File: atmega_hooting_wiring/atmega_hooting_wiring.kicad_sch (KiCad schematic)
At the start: 3 parts, among them U2 ATmega328-P

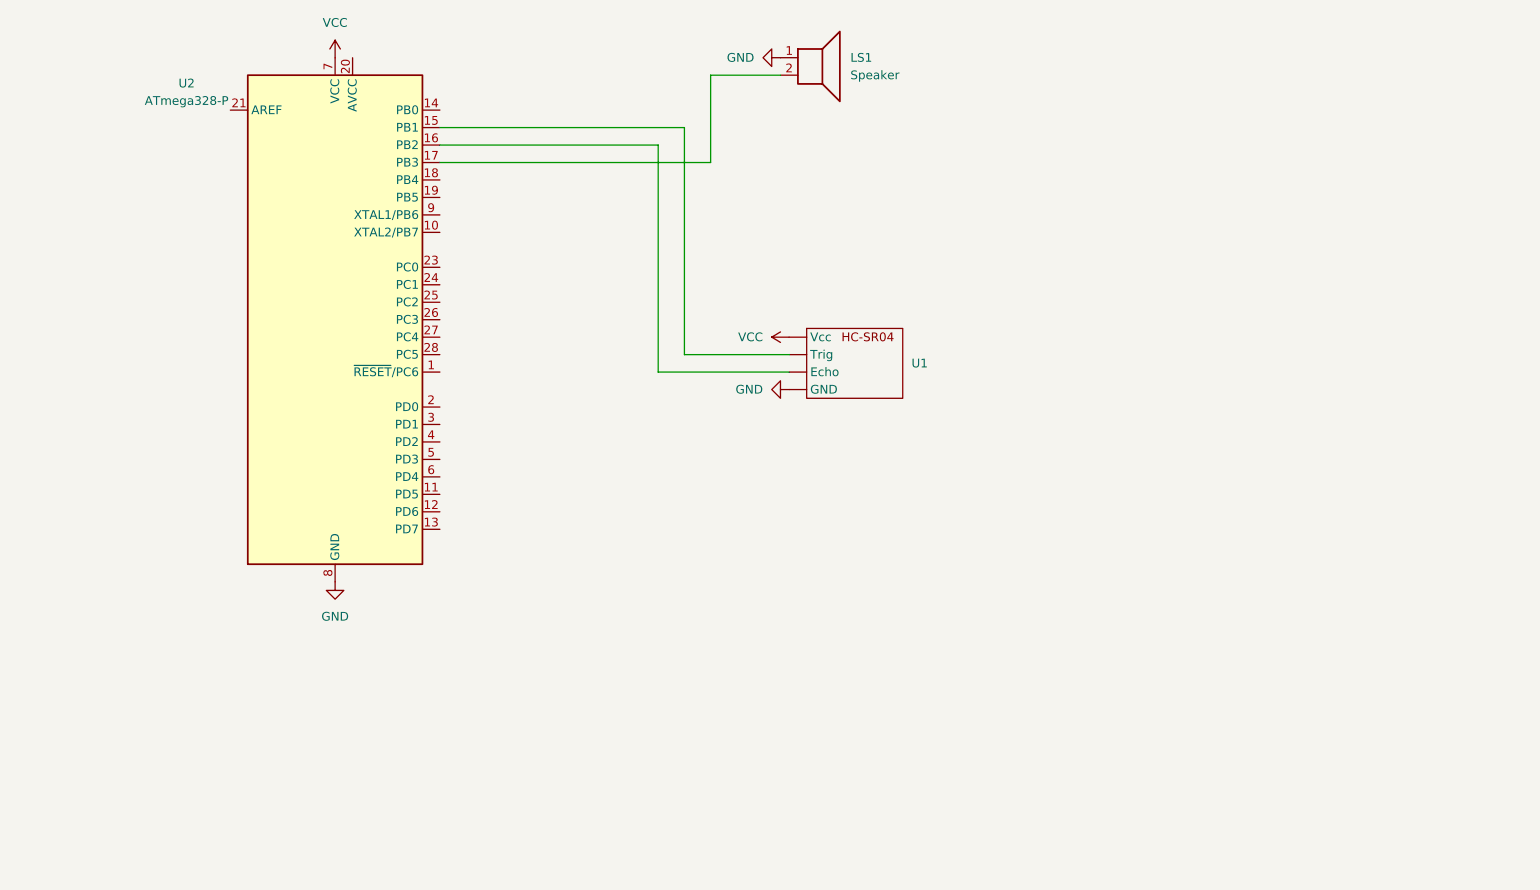
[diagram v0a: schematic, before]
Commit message: add pcb and wiring schematic for production
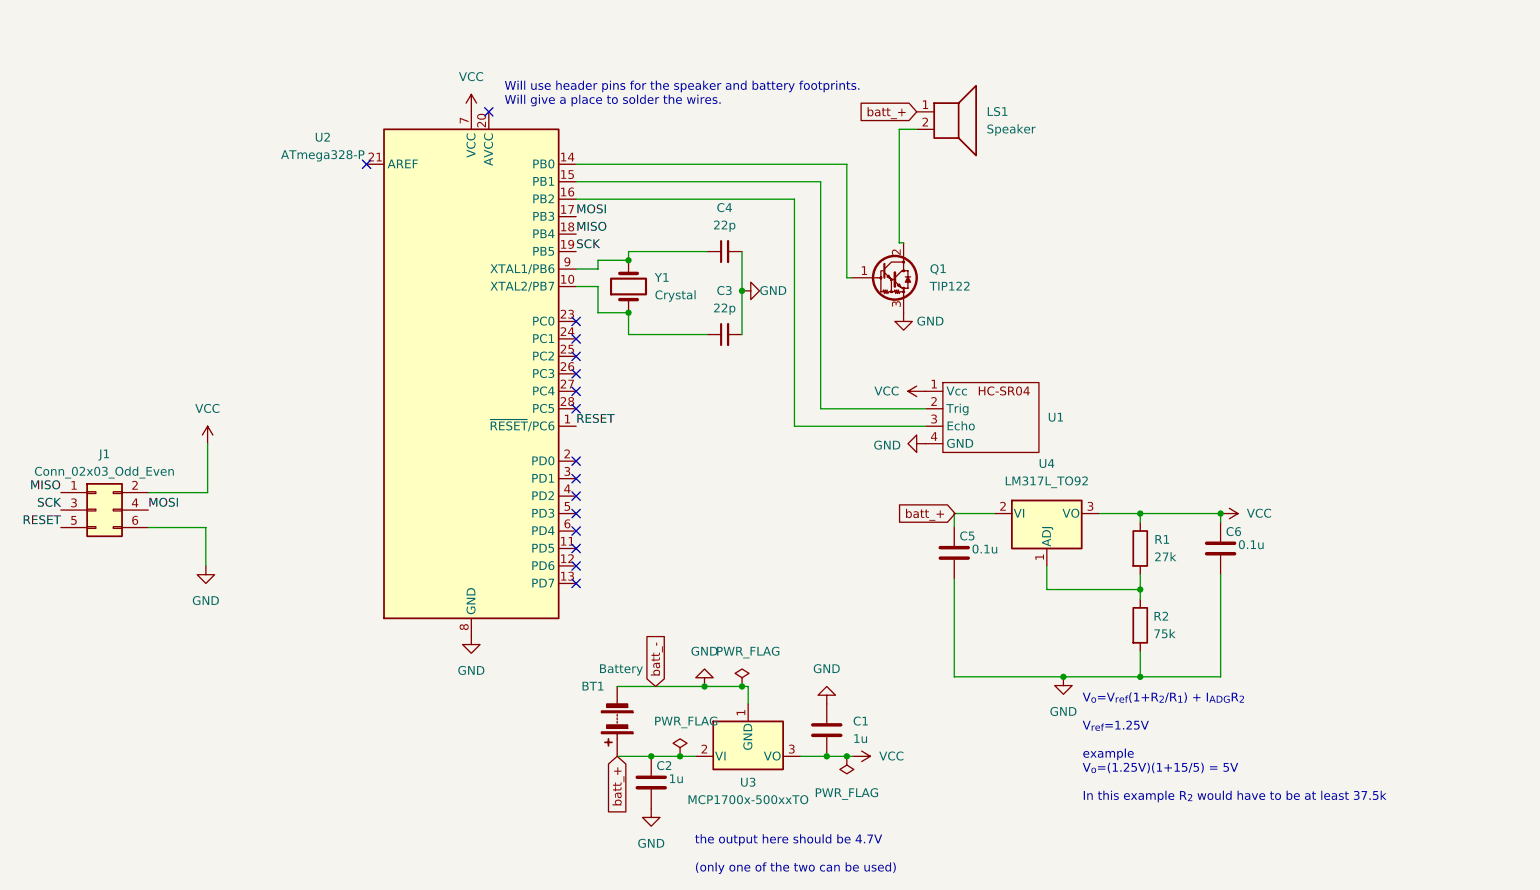
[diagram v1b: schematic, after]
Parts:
- added BT1: Battery, Connector_PinHeader_2.54mm:PinHeader_1x02_P2.54mm_Vertical, symbol Device:Battery
- added C1, C2: 1u, Capacitor_SMD:C_0805_2012Metric_Pad1.18x1.45mm_HandSolder, symbol Device:C
- added C3, C4: 22p, Capacitor_SMD:C_0805_2012Metric_Pad1.18x1.45mm_HandSolder, symbol Device:C_Small
- added C5, C6: 0.1u, Capacitor_SMD:C_0805_2012Metric_Pad1.18x1.45mm_HandSolder, symbol Device:C
- added J1: Conn_02x03_Odd_Even, symbol Connector_Generic:Conn_02x03_Odd_Even
- added Q1: TIP122, Package_TO_SOT_THT:TO-220-3_Vertical, symbol Transistor_BJT:TIP122
- added R1: 27k, Resistor_SMD:R_0805_2012Metric_Pad1.20x1.40mm_HandSolder, symbol Device:R
- added R2: 75k, Resistor_SMD:R_0805_2012Metric_Pad1.20x1.40mm_HandSolder, symbol Device:R
- added U3: MCP1700x-500xxTO, Package_TO_SOT_THT:TO-92_Inline, symbol Regulator_Linear:MCP1700x-500xxTO
- added U4: LM317L_TO92, Package_TO_SOT_THT:TO-92_Inline, symbol kody_custom_symbols:LM317L_TO92
- added Y1: Crystal, Crystal:Resonator-2Pin_W6.0mm_H3.0mm, symbol Device:Crystal
- LS1: footprint (none) -> Connector_PinHeader_2.54mm:PinHeader_1x02_P2.54mm_Vertical
- U1: footprint (none) -> Connector_PinHeader_2.54mm:PinHeader_1x04_P2.54mm_Vertical
- U2: MPN (none) -> ATMEGA328-PU
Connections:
- net GND: now also U1.4 (GND), BT1.2 (-), C1.1, C2.2, C3.2, C4.2, C5.2, C6.2, J1.6 (Pin_6), Q1.3 (E), R2.2, U3.1 (GND); no longer LS1.1, U1. (Vcc)
- net VCC: now also U1.1 (Vcc), C1.2, C6.1, J1.2 (Pin_2), R1.1, U3.3 (VO), U4.3 (VO); no longer U1. (Vcc)
- net at U2.15 (PB1): now also U1.2 (Trig); no longer U1. (Vcc)
- net at U2.16 (PB2): now also U1.3 (Echo); no longer U1. (Vcc)
- net RESET: now reaches U2.1 (~{RESET}/PC6)
- net RESET: now also J1.5 (Pin_5)
- net at U2.10 (XTAL2/PB7): now also C3.1, Y1.1
- net at U2.14 (PB0): now also Q1.1 (B)
- net at LS1.2: now also Q1.2 (C); no longer U2.17 (PB3)
- net MISO: now reaches U2.18 (PB4)
- net MISO: now also J1.1 (Pin_1)
- net SCK: now reaches U2.19 (PB5)
- net SCK: now also J1.3 (Pin_3)
- net at U2.9 (XTAL1/PB6): now also C4.1, Y1.2
- new net: R1.2, R2.1, U4.1 (ADJ)
- new net MOSI: J1.4 (Pin_4), U2.17 (PB3)
- new net batt_+: BT1.1 (+), C2.1, C5.1, LS1.1, U3.2 (VI), U4.2 (VI)
- no-connect marks 0 -> 16
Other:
- note added: "V_{o}=V_{ref}(1+R_{2}/R_{1}) + I_{ADG}R_{2} V_{ref}=1.25V example V_{o}=(1.25V)(1+15/5) = 5V In this example R_{2} would have to be at least 37.5k"
- note added: "Will use header pins for the speaker and battery footprints. Will give a place to solder the wires."
- note added: "the output here should be 4.7V (only one of the two can be used)"
- moved on the sheet: LS1, U2
